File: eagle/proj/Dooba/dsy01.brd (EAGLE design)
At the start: 66.2 x 70.1 mm, 90 parts, among them P1 DIO, P10 SWD_CORE(SWCLK-SWDIO-GND), P11 SWD_CORE(SWCLK-SWDIO-GND), P12 SWD(GND-RST), P2 CKI-CKO, P3 NOT, P4 RDY, P5 PWR(VIN-GND-RST), P6 SWD_CORE(SWCLK-SWDIO-GND), P7 SWD_CORE(SWCLK-SWDIO-GND)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

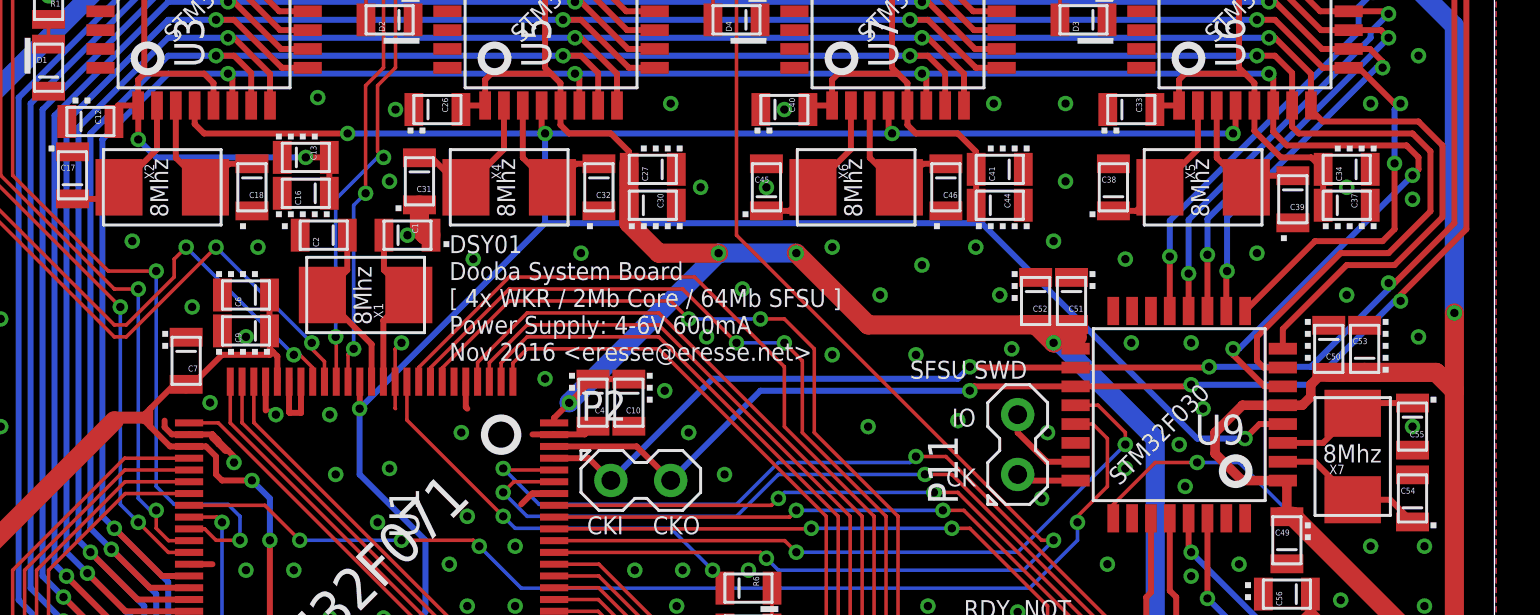
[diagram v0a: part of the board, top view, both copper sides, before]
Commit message: Completed DSY01 & DSD01-BSTA boards
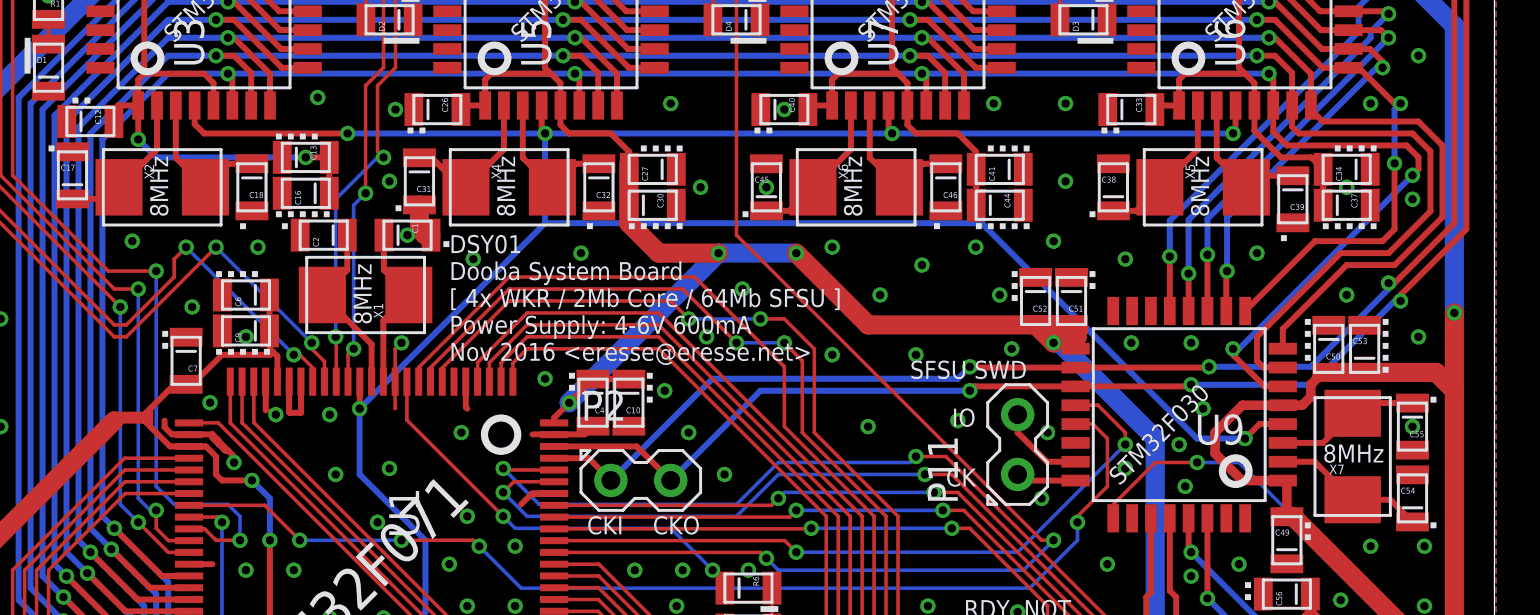
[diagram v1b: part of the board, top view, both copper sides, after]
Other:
- board text added: "8MHz"
- board text removed: "8Mhz"
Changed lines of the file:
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@@
 <text x="85.852" y="72.898" size="0.762" layer="21" font="vector" ratio="20" rot="R45">STM32F030</text>
 <text x="82.804" y="41.656" size="1.143" layer="21" font="vector" ratio="20">S25FL256S</text>
-<text x="50.038" y="60.96" size="0.762" layer="21" font="vector" ratio="20" rot="R90">8Mhz</text>
-<text x="41.402" y="65.532" size="0.762" layer="21" font="vector" ratio="20" rot="R90">8Mhz</text>
-<text x="56.134" y="65.532" size="0.762" layer="21" font="vector" ratio="20" rot="R90">8Mhz</text>
-<text x="70.866" y="65.532" size="0.762" layer="21" font="vector" ratio="20" rot="R90">8Mhz</text>
-<text x="85.598" y="65.532" size="0.762" layer="21" font="vector" ratio="20" rot="R90">8Mhz</text>
-<text x="90.424" y="55.118" size="0.762" layer="21" font="vector" ratio="20">8Mhz</text>
+<text x="50.038" y="60.96" size="0.762" layer="21" font="vector" ratio="20" rot="R90">8MHz</text>
+<text x="41.402" y="65.532" size="0.762" layer="21" font="vector" ratio="20" rot="R90">8MHz</text>
+<text x="56.134" y="65.532" size="0.762" layer="21" font="vector" ratio="20" rot="R90">8MHz</text>
+<text x="70.866" y="65.532" size="0.762" layer="21" font="vector" ratio="20" rot="R90">8MHz</text>
+<text x="85.598" y="65.532" size="0.762" layer="21" font="vector" ratio="20" rot="R90">8MHz</text>
+<text x="90.424" y="55.118" size="0.762" layer="21" font="vector" ratio="20">8MHz</text>
 <rectangle x1="72.369678125" y1="55.559959375" x2="77.830678125" y2="55.585359375" layer="22" rot="R180"/>
 <rectangle x1="72.344278125" y1="55.585359375" x2="77.856078125" y2="55.610759375" layer="22" rot="R180"/>
